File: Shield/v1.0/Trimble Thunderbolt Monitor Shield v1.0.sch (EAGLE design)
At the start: 31 parts, among them Q1 2N2222, U2 MAX232PTH

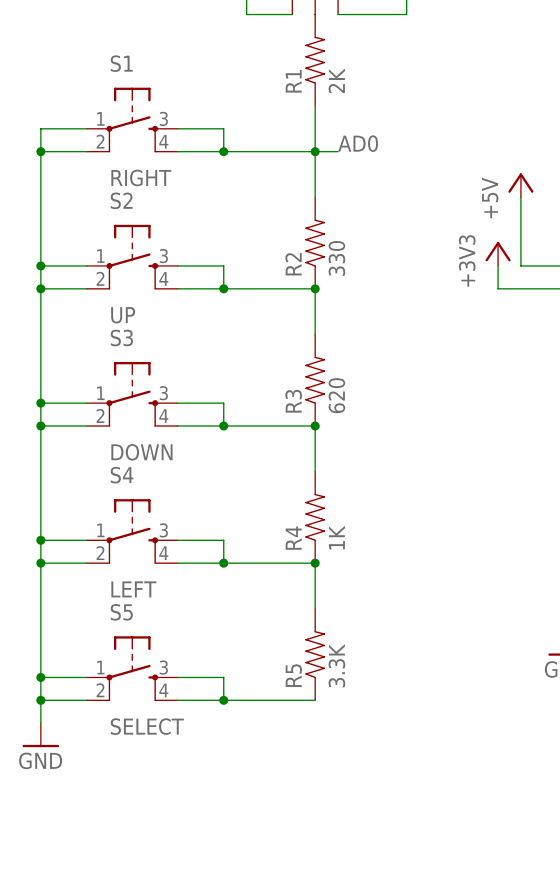
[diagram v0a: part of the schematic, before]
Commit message: Fixed some silkscreen issues
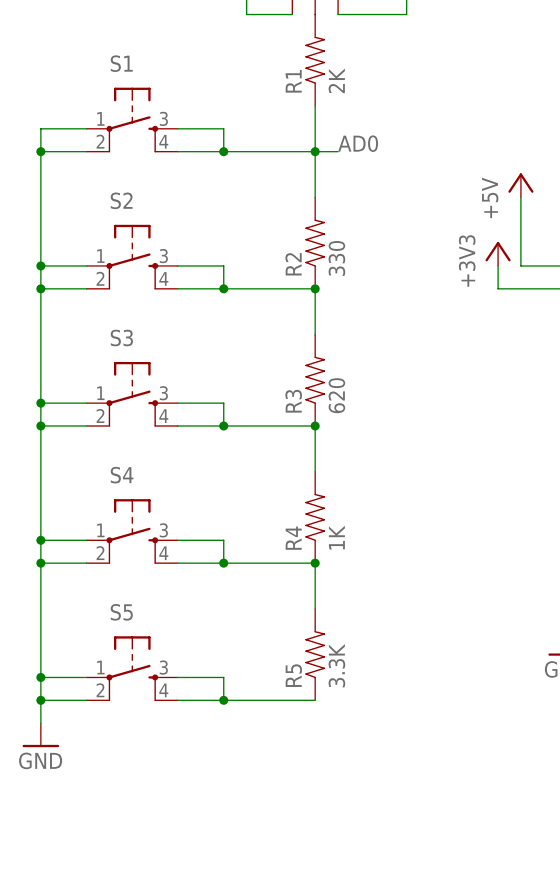
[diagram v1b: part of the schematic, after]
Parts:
- S1: value RIGHT -> (none)
- S2: value UP -> (none)
- S3: value DOWN -> (none)
- S4: value LEFT -> (none)
- S5: value SELECT -> (none)
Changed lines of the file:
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@@
 <?xml version="1.0" encoding="utf-8"?>
 <!DOCTYPE eagle SYSTEM "eagle.dtd">
-<eagle version="6.4">
+<eagle version="6.5.0">
 <drawing>
 <settings>
@@
 <part name="JP1" library="pinhead" deviceset="PINHD-1X16" device="" value="HD44780"/>
 <part name="U2" library="SparkFun" deviceset="MAX232" device="PTH"/>
-<part name="S2" library="SparkFun" deviceset="TAC_SWITCH" device="PTH" value="UP"/>
-<part name="S3" library="SparkFun" deviceset="TAC_SWITCH" device="PTH" value="DOWN"/>
-<part name="S4" library="SparkFun" deviceset="TAC_SWITCH" device="PTH" value="LEFT"/>
-<part name="S5" library="SparkFun" deviceset="TAC_SWITCH" device="PTH" value="SELECT"/>
+<part name="S2" library="SparkFun" deviceset="TAC_SWITCH" device="PTH"/>
+<part name="S3" library="SparkFun" deviceset="TAC_SWITCH" device="PTH"/>
+<part name="S4" library="SparkFun" deviceset="TAC_SWITCH" device="PTH"/>
+<part name="S5" library="SparkFun" deviceset="TAC_SWITCH" device="PTH"/>
 <part name="+3V1" library="supply1" deviceset="+3V3" device=""/>
 <part name="P+1" library="supply1" deviceset="+5V" device=""/>
@@
 <part name="C4" library="SparkFun" deviceset="CAP_POL" device="PTH2" value="1uF"/>
 <part name="GND9" library="supply1" deviceset="GND" device=""/>
-<part name="S1" library="SparkFun" deviceset="TAC_SWITCH" device="PTH" value="RIGHT"/>
+<part name="S1" library="SparkFun" deviceset="TAC_SWITCH" device="PTH"/>
 <part name="R9" library="SparkFun" deviceset="RESISTOR" device="AXIAL-0.3" value="330"/>
 <part name="R10" library="SparkFun" deviceset="RESISTOR" device="AXIAL-0.3" value="330"/>
